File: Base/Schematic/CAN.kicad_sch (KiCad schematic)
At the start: 8 parts, among them U3 CA-IS3052CW, U4 B0505S-1W

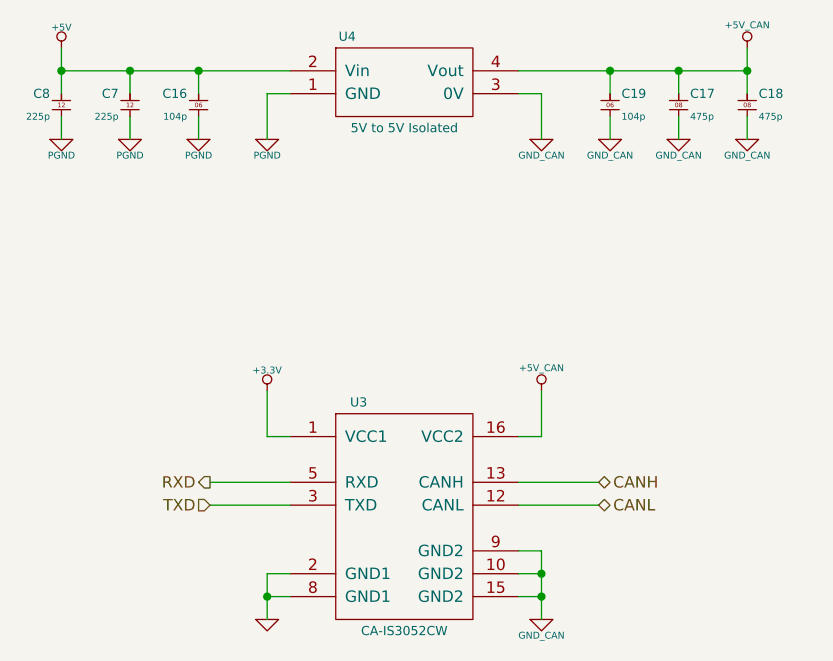
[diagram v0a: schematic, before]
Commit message: [Base 회로도 업데이트] - RS485, CAN 보호회로 추가
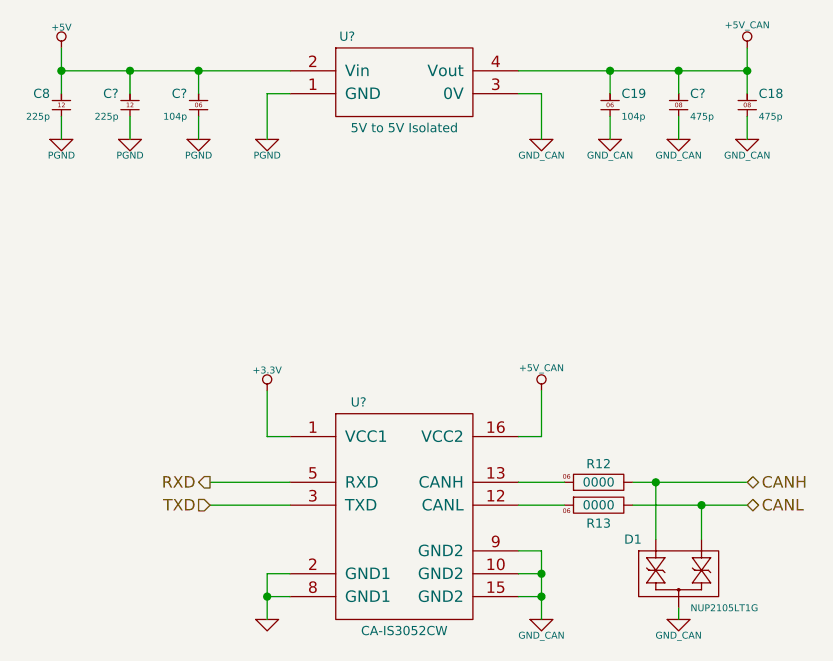
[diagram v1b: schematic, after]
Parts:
- added D1: NUP2105LT1G, SOT:SOT23, symbol Diode_Protection:NUP2105LT1G
- added R12, R13: WR06X0000JTL, SMR:0603, symbol Resistor:WR06X0000JTL
- renumbered C17 to C?, C7 to C?, C16 to C?, U4 to U?, U3 to U?
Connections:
- net CANH: now also D1.1 (A2), R12.2; no longer U?.13 (CANH)
- net CANL: now also D1.2 (C1), R13.2; no longer U?.12 (CANL)
- net GND_CAN: now also D1.3 (A1C2)
- new net: R12.1, U?.13 (CANH)
- new net: R13.1, U?.12 (CANL)

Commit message: [Base PCB 업데이트] - PCB 외곽선과 볼트 위치 설정
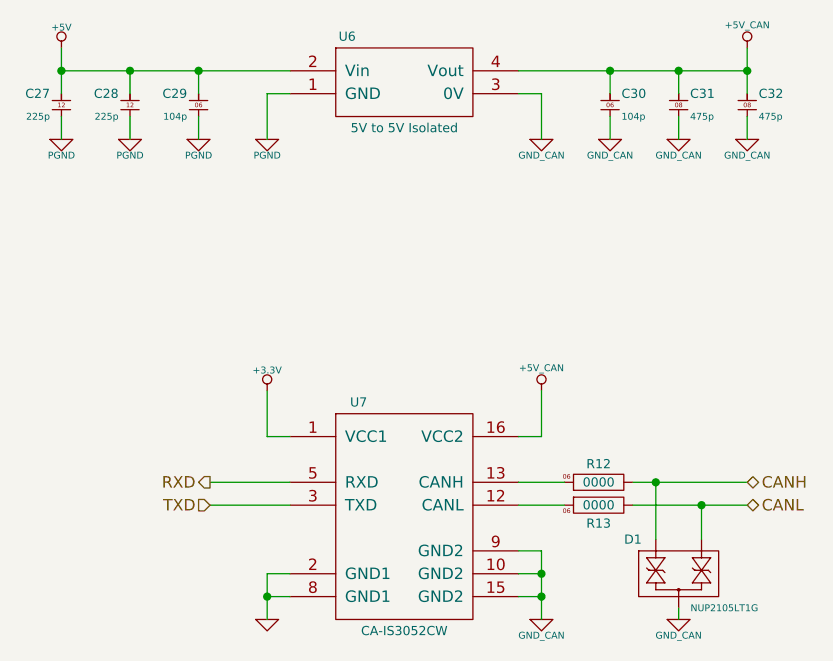
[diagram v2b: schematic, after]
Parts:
- gave numbers to parts that had none: 5
- renumbered C8 to C27, C19 to C30, C18 to C32
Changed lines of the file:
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@@
 		(dnp no)
 		(fields_autoplaced yes)
-		(property "Reference" "C18"
+		(property "Reference" "C32"
 			(at 189.23 69.85 0)
 			(do_not_autoplace yes)
@@
 			(project "Open-PLC-Project"
 				(path "/0d177ca6-e392-45a0-9514-d370436392ef/ecc73c34-7097-4317-902c-c1fb9ea56dcf"
-					(reference "C18")
+					(reference "C32")
 					(unit 1)
 				)
@@
 		(dnp no)
 		(fields_autoplaced yes)
-		(property "Reference" "#PWR031"
+		(property "Reference" "#PWR048"
 			(at 111.76 74.93 0)
 			(effects
@@
 			(project "Open-PLC-Project"
 				(path "/0d177ca6-e392-45a0-9514-d370436392ef/ecc73c34-7097-4317-902c-c1fb9ea56dcf"
-					(reference "#PWR031")
+					(reference "#PWR048")
 					(unit 1)
 				)
@@
 		(dnp no)
 		(fields_autoplaced yes)
-		(property "Reference" "C19"
+		(property "Reference" "C30"
 			(at 173.99 69.85 0)
 			(do_not_autoplace yes)
@@
 			(project "Open-PLC-Project"
 				(path "/0d177ca6-e392-45a0-9514-d370436392ef/ecc73c34-7097-4317-902c-c1fb9ea56dcf"
-					(reference "C19")
+					(reference "C30")
 					(unit 1)
 				)
@@
 		(dnp no)
 		(fields_autoplaced yes)
-		(property "Reference" "C?"
+		(property "Reference" "C31"
 			(at 181.61 69.85 0)
 			(do_not_autoplace yes)
@@
 			(project "Open-PLC-Project"
 				(path "/0d177ca6-e392-45a0-9514-d370436392ef/ecc73c34-7097-4317-902c-c1fb9ea56dcf"
-					(reference "C?")
+					(reference "C31")
 					(unit 1)
 				)
@@
 		(dnp no)
 		(fields_autoplaced yes)
-		(property "Reference" "C?"
+		(property "Reference" "C28"
 			(at 118.11 69.85 0)
 			(do_not_autoplace yes)
@@
 			(project "Open-PLC-Project"
 				(path "/0d177ca6-e392-45a0-9514-d370436392ef/ecc73c34-7097-4317-902c-c1fb9ea56dcf"
-					(reference "C?")
+					(reference "C28")
 					(unit 1)
 				)
@@
 		(dnp no)
 		(fields_autoplaced yes)
-		(property "Reference" "U?"
+		(property "Reference" "U6"
 			(at 143.51 63.5 0)
 			(do_not_autoplace yes)
@@
 			(project "Open-PLC-Project"
 				(path "/0d177ca6-e392-45a0-9514-d370436392ef/ecc73c34-7097-4317-902c-c1fb9ea56dcf"
-					(reference "U?")
+					(reference "U6")
 					(unit 1)
 				)
@@
 		(dnp no)
 		(fields_autoplaced yes)
-		(property "Reference" "#PWR017"
+		(property "Reference" "#PWR050"
 			(at 127 74.93 0)
 			(effects
@@
 			(project "Open-PLC-Project"
 				(path "/0d177ca6-e392-45a0-9514-d370436392ef/ecc73c34-7097-4317-902c-c1fb9ea56dcf"
-					(reference "#PWR017")
+					(reference "#PWR050")
 					(unit 1)
 				)
@@
 		(dnp no)
 		(fields_autoplaced yes)
-		(property "Reference" "#PWR?"
+		(property "Reference" "#PWR047"
 			(at 111.76 62.484 0)
 			(effects
@@
 			(project "Open-PLC-Project"
 				(path "/0d177ca6-e392-45a0-9514-d370436392ef/ecc73c34-7097-4317-902c-c1fb9ea56dcf"
-					(reference "#PWR?")
+					(reference "#PWR047")
 					(unit 1)
 				)
@@
 		(dnp no)
 		(fields_autoplaced yes)
-		(property "Reference" "C8"
+		(property "Reference" "C27"
 			(at 110.49 69.85 0)
 			(do_not_autoplace yes)
@@
 			(project "Open-PLC-Project"
 				(path "/0d177ca6-e392-45a0-9514-d370436392ef/ecc73c34-7097-4317-902c-c1fb9ea56dcf"
-					(reference "C8")
+					(reference "C27")
 					(unit 1)
 				)
@@
 		(dnp no)
 		(fields_autoplaced yes)
-		(property "Reference" "#PWR015"
+		(property "Reference" "#PWR051"
 			(at 134.62 74.93 0)
 			(effects
@@
 			(project "Open-PLC-Project"
 				(path "/0d177ca6-e392-45a0-9514-d370436392ef/ecc73c34-7097-4317-902c-c1fb9ea56dcf"
-					(reference "#PWR015")
+					(reference "#PWR051")
 					(unit 1)
 				)
@@
 		(dnp no)
 		(fields_autoplaced yes)
-		(property "Reference" "C?"
+		(property "Reference" "C29"
 			(at 125.73 69.85 0)
 			(do_not_autoplace yes)
@@
 			(project "Open-PLC-Project"
 				(path "/0d177ca6-e392-45a0-9514-d370436392ef/ecc73c34-7097-4317-902c-c1fb9ea56dcf"
-					(reference "C?")
+					(reference "C29")
 					(unit 1)
 				)
@@
 		(dnp no)
 		(fields_autoplaced yes)
-		(property "Reference" "#GND_CAN04"
+		(property "Reference" "#GND_CAN02"
 			(at 165.1 128.27 0)
 			(effects
@@
 			(project "Open-PLC-Project"
 				(path "/0d177ca6-e392-45a0-9514-d370436392ef/ecc73c34-7097-4317-902c-c1fb9ea56dcf"
-					(reference "#GND_CAN04")
+					(reference "#GND_CAN02")
 					(unit 1)
 				)
@@
 		(dnp no)
 		(fields_autoplaced yes)
-		(property "Reference" "#PWR030"
+		(property "Reference" "#PWR049"
 			(at 119.38 74.93 0)
 			(effects
@@
 			(project "Open-PLC-Project"
 				(path "/0d177ca6-e392-45a0-9514-d370436392ef/ecc73c34-7097-4317-902c-c1fb9ea56dcf"
-					(reference "#PWR030")
+					(reference "#PWR049")
 					(unit 1)
 				)
@@
 		(dnp no)
 		(fields_autoplaced yes)
-		(property "Reference" "#GND_CAN03"
+		(property "Reference" "#GND_CAN06"
 			(at 187.96 74.93 0)
 			(effects
@@
 			(project "Open-PLC-Project"
 				(path "/0d177ca6-e392-45a0-9514-d370436392ef/ecc73c34-7097-4317-902c-c1fb9ea56dcf"
-					(reference "#GND_CAN03")
+					(reference "#GND_CAN06")
 					(unit 1)
 				)
@@
 		(dnp no)
 		(fields_autoplaced yes)
-		(property "Reference" "U?"
+		(property "Reference" "U7"
 			(at 144.78 104.14 0)
 			(do_not_autoplace yes)
@@
 			(project "Open-PLC-Project"
 				(path "/0d177ca6-e392-45a0-9514-d370436392ef/ecc73c34-7097-4317-902c-c1fb9ea56dcf"
-					(reference "U?")
+					(reference "U7")
 					(unit 1)
 				)
@@
 		(dnp no)
 		(fields_autoplaced yes)
-		(property "Reference" "#PWR?"
+		(property "Reference" "#PWR053"
 			(at 134.62 128.27 0)
 			(effects
@@
 			(project "Open-PLC-Project"
 				(path "/0d177ca6-e392-45a0-9514-d370436392ef/ecc73c34-7097-4317-902c-c1fb9ea56dcf"
-					(reference "#PWR?")
+					(reference "#PWR053")
 					(unit 1)
 				)
@@
 		(dnp no)
 		(fields_autoplaced yes)
-		(property "Reference" "#GND_CAN01"
+		(property "Reference" "#GND_CAN03"
 			(at 172.72 74.93 0)
 			(effects
@@
 			(project "Open-PLC-Project"
 				(path "/0d177ca6-e392-45a0-9514-d370436392ef/ecc73c34-7097-4317-902c-c1fb9ea56dcf"
-					(reference "#GND_CAN01")
+					(reference "#GND_CAN03")
 					(unit 1)
 				)
@@
 		(dnp no)
 		(fields_autoplaced yes)
-		(property "Reference" "#GND_CAN"
+		(property "Reference" "#GND_CAN01"
 			(at 165.1 74.93 0)
 			(effects
@@
 			(project ""
 				(path "/0d177ca6-e392-45a0-9514-d370436392ef/ecc73c34-7097-4317-902c-c1fb9ea56dcf"
-					(reference "#GND_CAN")
+					(reference "#GND_CAN01")
 					(unit 1)
 				)
@@
 		(dnp no)
 		(fields_autoplaced yes)
-		(property "Reference" "#GND_CAN02"
+		(property "Reference" "#GND_CAN04"
 			(at 180.34 74.93 0)
 			(effects
@@
 			(project "Open-PLC-Project"
 				(path "/0d177ca6-e392-45a0-9514-d370436392ef/ecc73c34-7097-4317-902c-c1fb9ea56dcf"
-					(reference "#GND_CAN02")
+					(reference "#GND_CAN04")
 					(unit 1)
 				)
@@
 		(on_board yes)
 		(dnp no)
-		(property "Reference" "#5V_CAN"
+		(property "Reference" "#5V_CAN02"
 			(at 187.96 62.484 0)
 			(effects
@@
 			(project ""
 				(path "/0d177ca6-e392-45a0-9514-d370436392ef/ecc73c34-7097-4317-902c-c1fb9ea56dcf"
-					(reference "#5V_CAN")
+					(reference "#5V_CAN02")
 					(unit 1)
 				)
@@
 		(dnp no)
 		(fields_autoplaced yes)
-		(property "Reference" "#PWR?"
+		(property "Reference" "#PWR052"
 			(at 134.62 100.584 0)
 			(effects
@@
 			(project "Open-PLC-Project"
 				(path "/0d177ca6-e392-45a0-9514-d370436392ef/ecc73c34-7097-4317-902c-c1fb9ea56dcf"
-					(reference "#PWR?")
-					(unit 1)
-				)
+					(reference "#PWR052")
+					(unit 1)
+				)

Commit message: [Base 회로도 업데이트] - AIN 입력 4개 추가
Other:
- company: (none) -> -
- title: (none) -> Open-PLC-Project
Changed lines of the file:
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@@
 	(generator_version "8.0")
 	(paper "A4")
+	(title_block
+		(title "Open-PLC-Project")
+		(date "2024-12-01")
+		(company "-")
+		(comment 1 "See the file \"LICENSE\" in the main directory of this archive for more details.")
+		(comment 2 "This file is subject to the terms and conditions of the MIT License.")
+		(comment 3 "Copyright (c) 2024 Yoon-Ki Hong")
+	)
 	(junction
 		(at 165.1 125.73)
@@
 		(dnp no)
 		(fields_autoplaced yes)
-		(property "Reference" "#PWR048"
+		(property "Reference" "#PWR057"
 			(at 111.76 74.93 0)
 			(effects
@@
 			(project "Open-PLC-Project"
 				(path "/0d177ca6-e392-45a0-9514-d370436392ef/ecc73c34-7097-4317-902c-c1fb9ea56dcf"
-					(reference "#PWR048")
+					(reference "#PWR057")
 					(unit 1)
 				)
@@
 		(dnp no)
 		(fields_autoplaced yes)
-		(property "Reference" "#PWR050"
+		(property "Reference" "#PWR059"
 			(at 127 74.93 0)
 			(effects
@@
 			(project "Open-PLC-Project"
 				(path "/0d177ca6-e392-45a0-9514-d370436392ef/ecc73c34-7097-4317-902c-c1fb9ea56dcf"
-					(reference "#PWR050")
+					(reference "#PWR059")
 					(unit 1)
 				)
@@
 		(dnp no)
 		(fields_autoplaced yes)
-		(property "Reference" "#PWR047"
+		(property "Reference" "#PWR056"
 			(at 111.76 62.484 0)
 			(effects
@@
 			(project "Open-PLC-Project"
 				(path "/0d177ca6-e392-45a0-9514-d370436392ef/ecc73c34-7097-4317-902c-c1fb9ea56dcf"
-					(reference "#PWR047")
+					(reference "#PWR056")
 					(unit 1)
 				)
@@
 		(dnp no)
 		(fields_autoplaced yes)
-		(property "Reference" "#PWR051"
+		(property "Reference" "#PWR060"
 			(at 134.62 74.93 0)
 			(effects
@@
 			(project "Open-PLC-Project"
 				(path "/0d177ca6-e392-45a0-9514-d370436392ef/ecc73c34-7097-4317-902c-c1fb9ea56dcf"
-					(reference "#PWR051")
+					(reference "#PWR060")
 					(unit 1)
 				)
@@
 		(dnp no)
 		(fields_autoplaced yes)
-		(property "Reference" "#PWR049"
+		(property "Reference" "#PWR058"
 			(at 119.38 74.93 0)
 			(effects
@@
 			(project "Open-PLC-Project"
 				(path "/0d177ca6-e392-45a0-9514-d370436392ef/ecc73c34-7097-4317-902c-c1fb9ea56dcf"
-					(reference "#PWR049")
+					(reference "#PWR058")
 					(unit 1)
 				)
@@
 		(dnp no)
 		(fields_autoplaced yes)
-		(property "Reference" "#PWR053"
+		(property "Reference" "#PWR062"
 			(at 134.62 128.27 0)
 			(effects
@@
 			(project "Open-PLC-Project"
 				(path "/0d177ca6-e392-45a0-9514-d370436392ef/ecc73c34-7097-4317-902c-c1fb9ea56dcf"
-					(reference "#PWR053")
+					(reference "#PWR062")
 					(unit 1)
 				)
@@
 		(dnp no)
 		(fields_autoplaced yes)
-		(property "Reference" "#PWR052"
+		(property "Reference" "#PWR061"
 			(at 134.62 100.584 0)
 			(effects
@@
 			(project "Open-PLC-Project"
 				(path "/0d177ca6-e392-45a0-9514-d370436392ef/ecc73c34-7097-4317-902c-c1fb9ea56dcf"
-					(reference "#PWR052")
-					(unit 1)
-				)
+					(reference "#PWR061")
+					(unit 1)
+				)
